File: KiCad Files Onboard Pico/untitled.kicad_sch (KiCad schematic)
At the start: 42 parts, among them J2 GT-USB-7051A, J3 Button, J4 TYPE-C-31-M-12, U2 TPS63001DRCR, U4 RP2040, Y1 3225_4P 12MHz

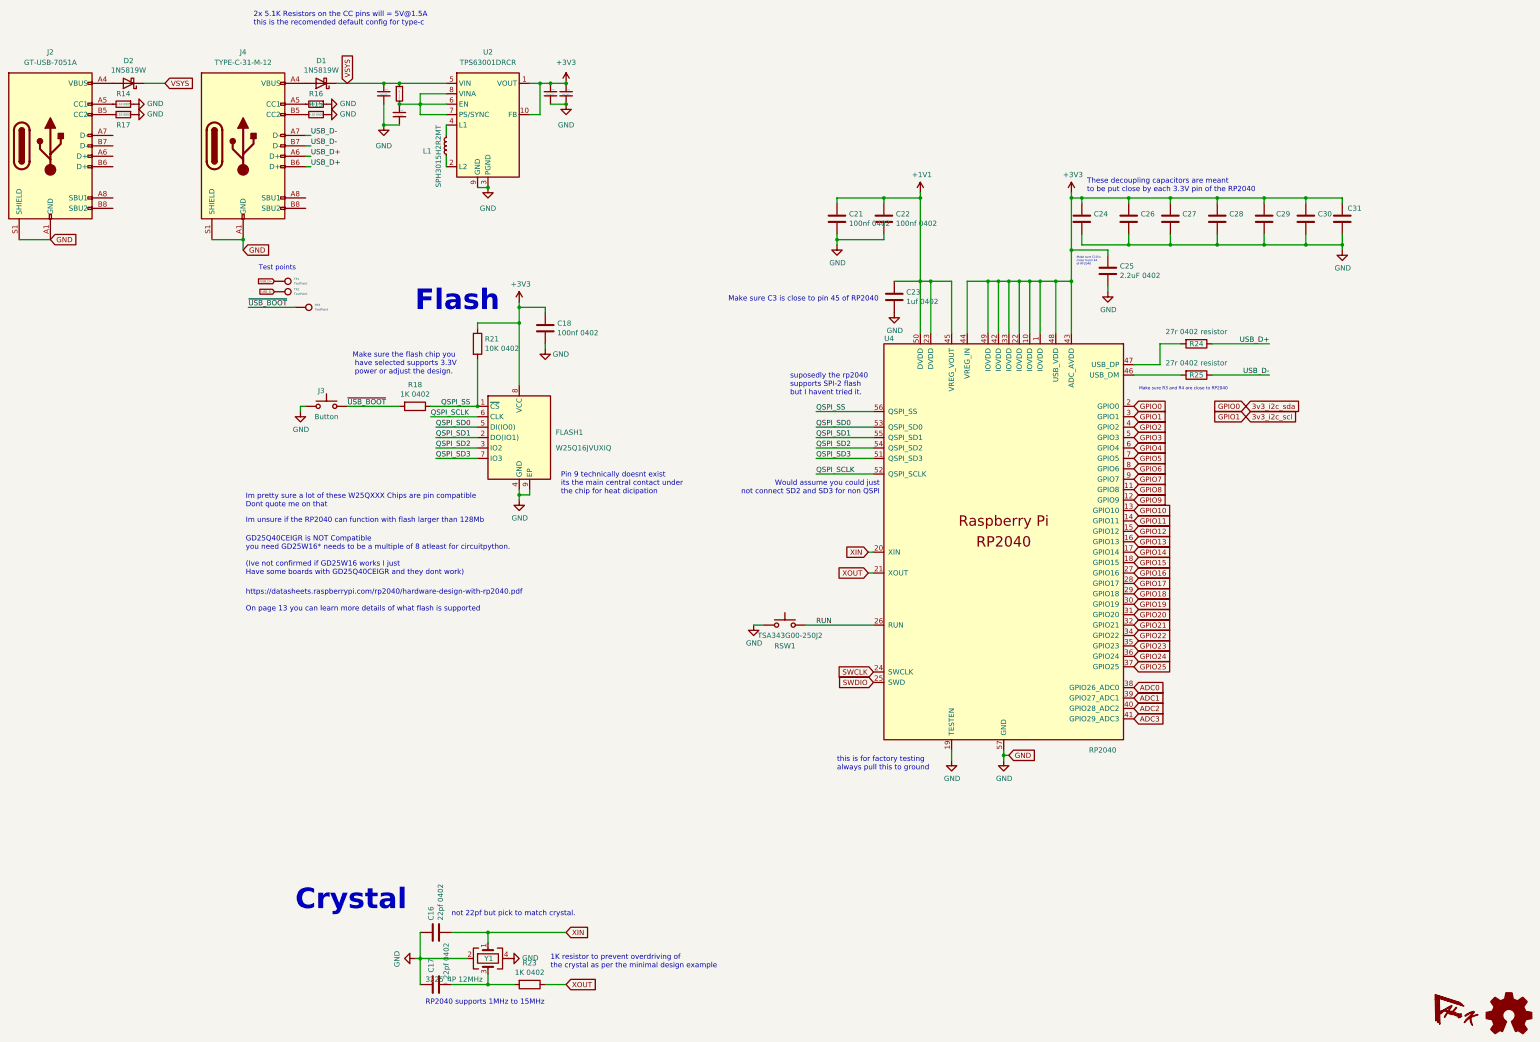
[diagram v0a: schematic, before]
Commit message: removed sockets, added level shifter IC, changed RTC to smaller package, re-did entire board to be more tidy.
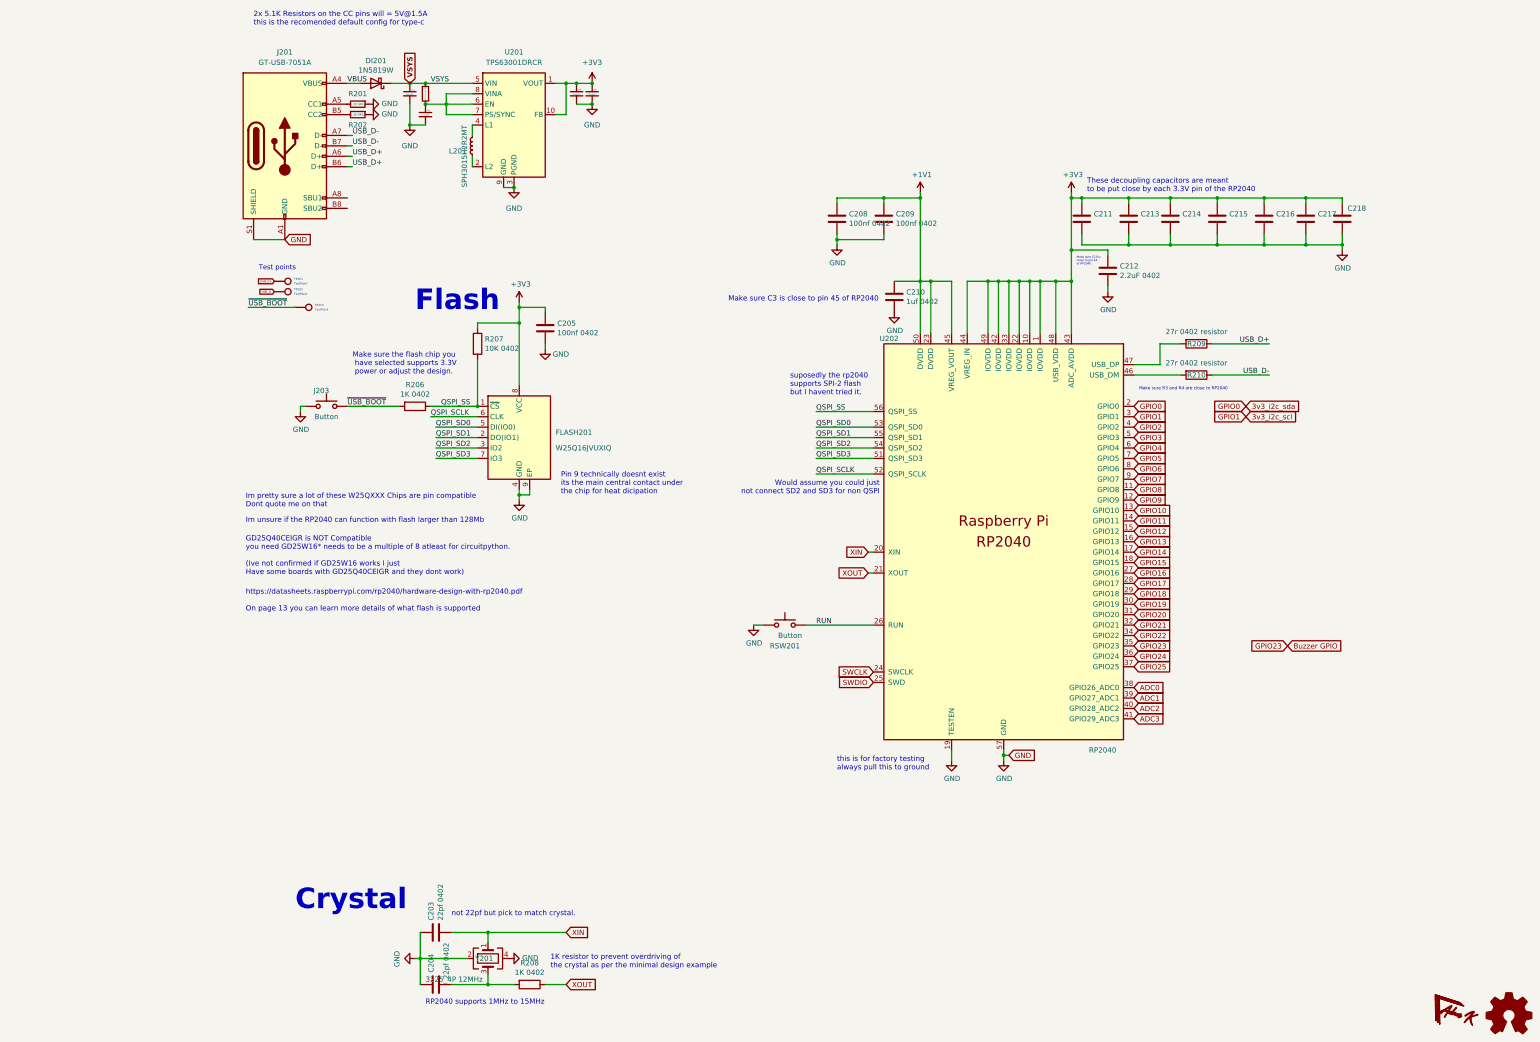
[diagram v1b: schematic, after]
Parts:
- removed D1: 1N5819W, Diode_SMD:D_SOD-123, symbol Device:D_Schottky
- removed J4: TYPE-C-31-M-12, Connector_USB:USB_C_Receptacle_HRO_TYPE-C-31-M-12, symbol Connector:USB_C_Receptacle_USB2.0_16P
- removed R15, R16: 5.1K 0402, Resistor_SMD:R_0402_1005Metric, symbol Device:R_Small
- J203: renamed from J3; footprint Button_Switch_SMD:SW_Push_SPST_NO_Alps_SKRK -> Button_Switch_SMD:SW_SPST_B3U-1000P-B
- R201: renamed from R14; value 5.1K 0805 -> 5.1K 0402; footprint Resistor_SMD:R_0805_2012Metric -> Resistor_SMD:R_0402_1005Metric
- R202: renamed from R17; value 5.1K 0805 -> 5.1K 0402; footprint Resistor_SMD:R_0805_2012Metric -> Resistor_SMD:R_0402_1005Metric
- RSW201: renamed from RSW1; value TSA343G00-250J2 -> Button; footprint Button_Switch_SMD:SW_Push_SPST_NO_Alps_SKRK -> Button_Switch_SMD:SW_SPST_B3U-1000P-B
- renumbered C15 to C201, C19 to C202, C16 to C203, C17 to C204, C18 to C205, C20 to C206, C32 to C207, C21 to C208, C22 to C209, C23 to C210, C24 to C211, C25 to C212, C26 to C213, C27 to C214, C28 to C215, C29 to C216, C30 to C217, C31 to C218, D2 to DI201, FLASH1 to FLASH201, J2 to J201, L1 to L201, R19 to R205, R18 to R206, R21 to R207, R23 to R208, R24 to R209, R25 to R210, TP1 to TP201, TP2 to TP202, TP3 to TP203, U2 to U201, U4 to U202, Y1 to Y201
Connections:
- net USB_D+: now also J201.A6 (D+), J201.B6 (D+)
- net USB_D-: now also J201.A7 (D-), J201.B7 (D-)
- net VBUS: now reaches DI201.2 (A), J201.A4 (VBUS), J201.A9 (VBUS), J201.B4 (VBUS), J201.B9 (VBUS)
- net GPIO23 renamed Buzzer GPIO
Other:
- moved on the sheet: C201, C202, C206, C207, DI201, J201, L201, R201, R202, R205, U201
